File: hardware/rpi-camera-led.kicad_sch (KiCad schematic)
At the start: 20 parts, among them J1 FFC 15P 1.0mm bottom contact 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, J2 FFC 15P 1.0mm top contact (to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, J3 Qwiic (JST SH 1.0mm), J4 SWD program header 2.54mm, Q1 AO3400A, Q2 Phototransistor, U1 CH32V003A4M6

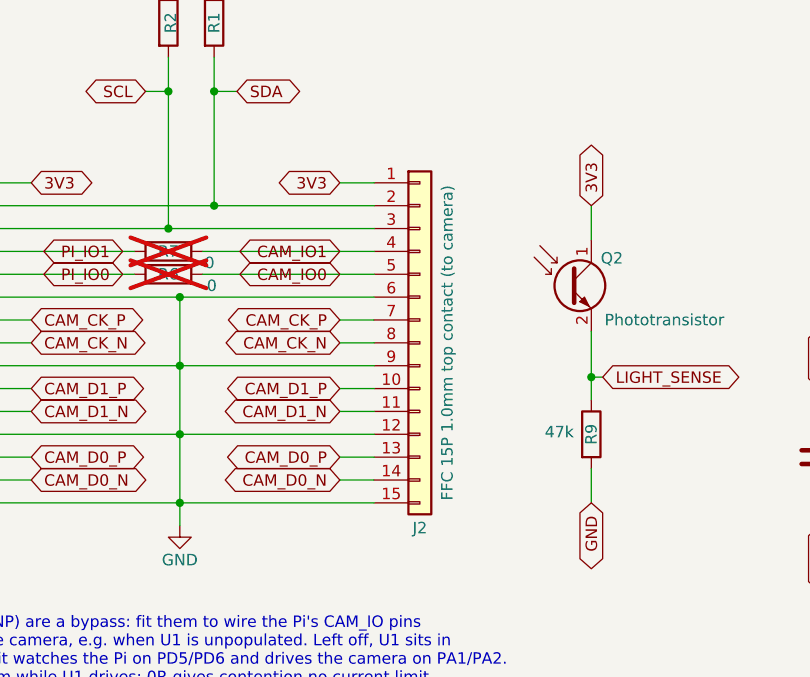
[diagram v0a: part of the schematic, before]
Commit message: Tim's KiCad session: six straight MIPI runs, J2 re-mirrored
Committing the working files as they stand so the routing is not lost.
This is an inconsistent intermediate state, recorded rather than
tidied, because the two halves disagree:

  * Six straight traces on F.Cu, 0.2mm, each a full 12.6mm run at
    constant Y from J1's pad column to J2's -- the MIPI pairs and
    clock, exactly the payoff the alignment work was for.
  * J2 carries (mirror x) again, which puts the connector mapping back
    to J1.k <-> J2.k and undoes be3c223.

Straight runs need the reversed mapping, so with the mirror back five
of the six traces land on a pad of the wrong net: CAM_CK_P on J2.7
(GND), CAM_D0_N on J2.14 (SDA), CAM_D0_P on J2.13 (SCL), CAM_D1_N on
J2.11 (CAM_IO0), CAM_D1_P on J2.10 (GND).  Only CAM_CK_N is right, pin
8 being the one pin where both mappings agree.  Hence DRC 93 -> 111 and
one net fewer unconnected.

Everything else from the recent commits survived the save, so this
looks like the schematic editor writing back a buffer loaded before
be3c223 rather than a decision.

Co-Authored-By: Claude Opus 5 (1M context) <noreply@anthropic.com>
Claude-Session: https://claude.ai/code/session_01E6VQHygrbAGSqdngQQsBdx
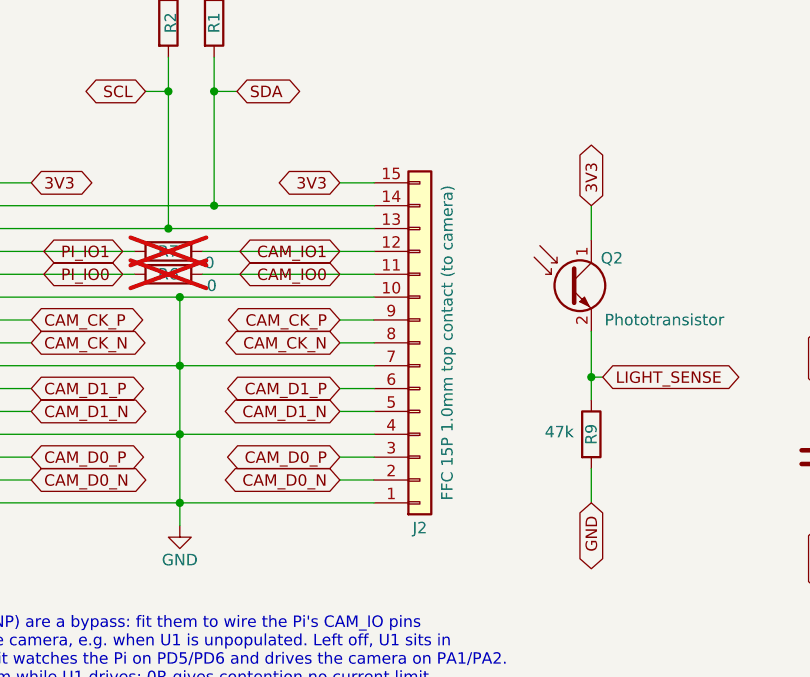
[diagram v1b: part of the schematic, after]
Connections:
- net 3V3: now also J2.15 (Pin_15); no longer J2.1 (Pin_1)
- net CAM_CK_P: now also J2.9 (Pin_9); no longer J2.7 (Pin_7)
- net CAM_D0_N: now also J2.2 (Pin_2); no longer J2.14 (Pin_14)
- net CAM_D0_P: now also J2.3 (Pin_3); no longer J2.13 (Pin_13)
- net CAM_D1_N: now also J2.5 (Pin_5); no longer J2.11 (Pin_11)
- net CAM_D1_P: now also J2.6 (Pin_6); no longer J2.10 (Pin_10)
- net CAM_IO0: now also J2.11 (Pin_11); no longer J2.5 (Pin_5)
- net CAM_IO1: now also J2.12 (Pin_12); no longer J2.4 (Pin_4)
- net GND: now also J2.1 (Pin_1), J2.10 (Pin_10), J2.4 (Pin_4), J2.7 (Pin_7); no longer J2.12 (Pin_12), J2.15 (Pin_15), J2.6 (Pin_6), J2.9 (Pin_9)
- net SCL: now also J2.13 (Pin_13); no longer J2.3 (Pin_3)
- net SDA: now also J2.14 (Pin_14); no longer J2.2 (Pin_2)
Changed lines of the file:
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@@
 		)
 	)
+	(text "J1 and J2 are deliberately different parts: J1 bottom contact, J2 top contact.\nTop contact mirrors J2's cable-to-pad order, which cancels the 180 deg rotation\nbetween two connectors whose cables leave opposite edges -- so every J1->J2 net\nruns straight across on one layer instead of crossing the whole bus.\nCost: the camera-side cable goes in contacts up, i.e. flipped from the Pi side.\nUse an opposite-side (type D) FFC there, or fold a standard same-side one."
+		(exclude_from_sim no)
+		(at 181.61 149.86 0)
+		(effects
+			(font
+				(size 1.27 1.27)
+			)
+			(justify left bottom)
+		)
+	)
 	(text "SOP-16 bonds no two ports to one pin, so PD1/SWIO is programming only\nand PC3/T1CH3 drives the LED gate: no LED flicker while flashing firmware.\nPC6, PC7, PD4 and PC0 are spare. PD7 is left unused on purpose: it is NRST\nuntil the RST_MODE option byte says otherwise, so a Pi GPIO on it would\nreset the MCU on a factory-fresh part."
 		(exclude_from_sim no)
@@
 		(at 160.02 52.07)
 	)
+	(no_connect
+		(at 160.02 59.69)
+	)
 	(wire
 		(pts
@@
 	(wire
 		(pts
+			(xy 160.02 54.61) (xy 163.83 54.61)
+		)
+		(stroke
+			(width 0)
+			(type default)
+		)
+	)
+	(wire
+		(pts
 			(xy 27.94 74.93) (xy 43.18 74.93)
 		)
@@
 		)
 	)
+	(global_label "PI_IO1"
+		(shape bidirectional)
+		(at 163.83 54.61 0)
+		(fields_autoplaced yes)
+		(effects
+			(font
+				(size 1.27 1.27)
+			)
+			(justify left)
+		)
+		(property "Intersheetrefs" "${INTERSHEET_REFS}"
+			(at 173.9137 54.61 0)
+			(effects
+				(font
+					(size 1.27 1.27)
+				)
+				(justify left)
+				(hide yes)
+			)
+		)
+	)
 	(global_label "GND"
 		(shape bidirectional)
@@
 		(lib_id "Connector_Generic:Conn_01x15")
 		(at 74.93 82.55 0)
+		(mirror x)
 		(unit 1)
 		(exclude_from_sim no)
@@
 	)
 	(embedded_fonts no)
-	(wire
-		(pts
-			(xy 160.02 54.61) (xy 163.83 54.61)
-		)
-		(stroke
-			(width 0)
-			(type default)
-		)
-	)
-	(global_label "PI_IO1"
-		(shape bidirectional)
-		(at 163.83 54.61 0)
-		(fields_autoplaced yes)
-		(effects
-			(font
-				(size 1.27 1.27)
-			)
-			(justify left)
-		)
-		(property "Intersheetrefs" "${INTERSHEET_REFS}"
-			(at 173.9137 54.61 0)
-			(effects
-				(font
-					(size 1.27 1.27)
-				)
-				(justify left)
-				(hide yes)
-			)
-		)
-	)
-	(no_connect
-		(at 160.02 59.69)
-	)
-	(text "J1 and J2 are deliberately different parts: J1 bottom contact, J2 top contact.\nTop contact mirrors J2's cable-to-pad order, which cancels the 180 deg rotation\nbetween two connectors whose cables leave opposite edges -- so every J1->J2 net\nruns straight across on one layer instead of crossing the whole bus.\nCost: the camera-side cable goes in contacts up, i.e. flipped from the Pi side.\nUse an opposite-side (type D) FFC there, or fold a standard same-side one."
-		(exclude_from_sim no)
-		(at 181.61 149.86 0)
-		(effects
-			(font
-				(size 1.27 1.27)
-			)
-			(justify left bottom)
-		)
-	)
 )

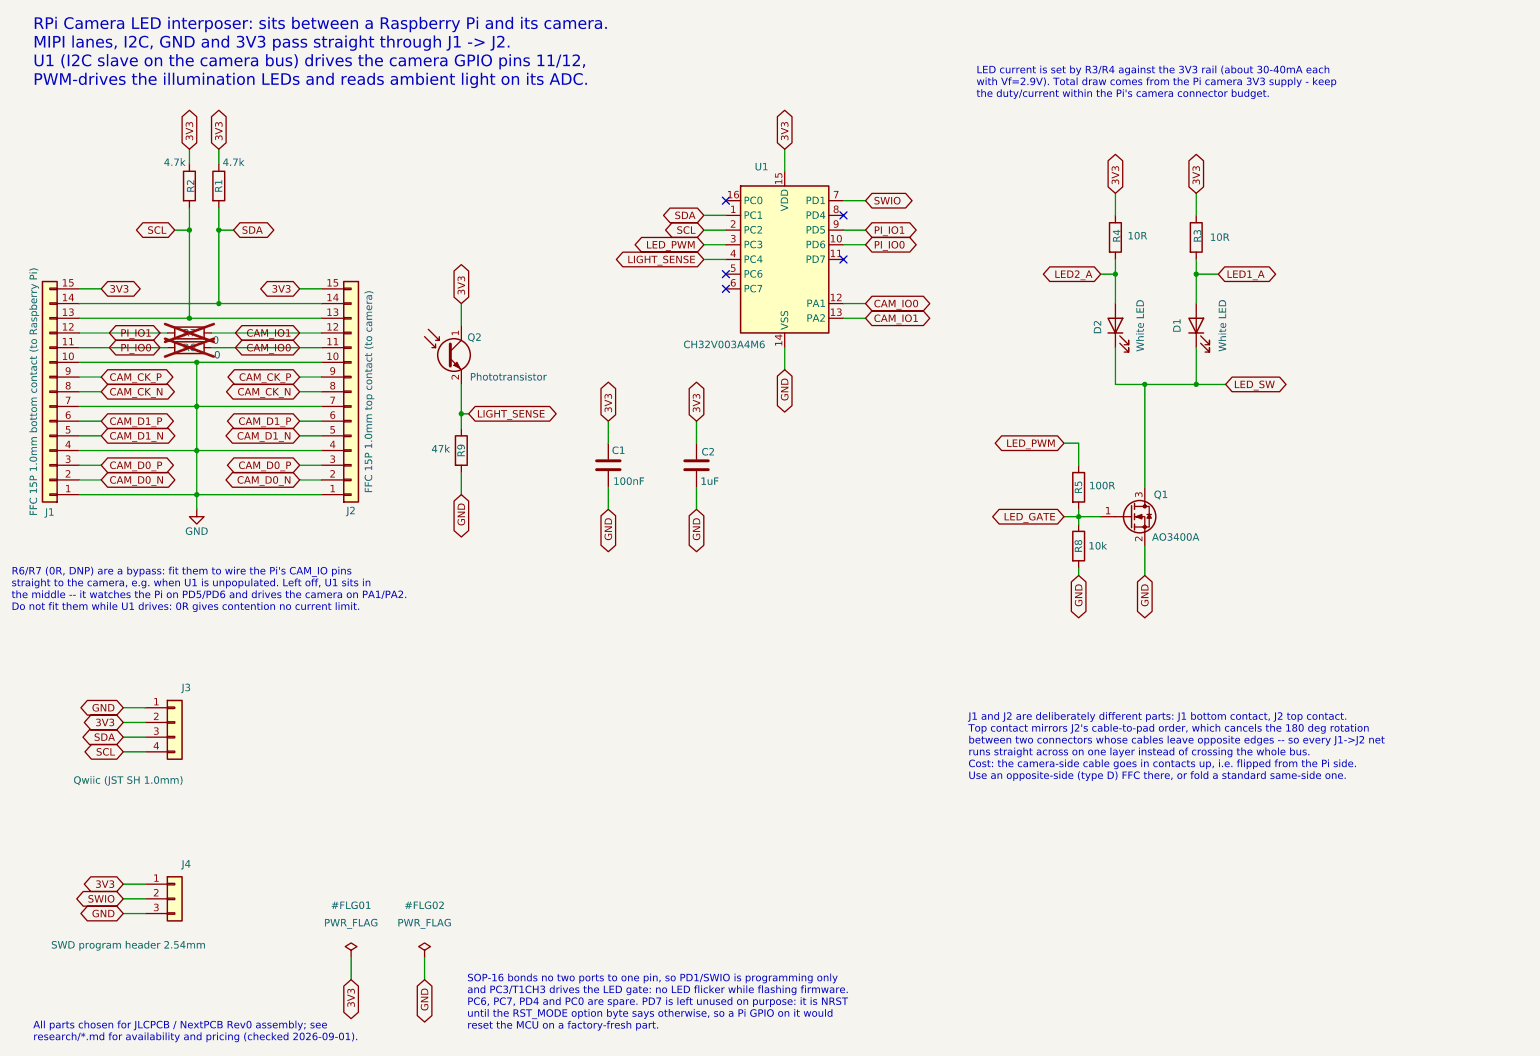
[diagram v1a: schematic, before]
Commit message: Put J2 back on the original bottom-contact part
Undo a708eef and be3c223: J1 and J2 are the same AFA07-S15FCA-00
again, wired pin-for-pin, so a standard same-side Raspberry Pi camera
cable works at both ends.  That was the real cost of the top-contact
route -- it needed an opposite-side (type D) FFC or a fold on the
camera segment, which is a poor trade for a board whose point is to sit
transparently in an existing cable run.

Everything that existed only to support the swap goes with it: the
project footprint library holding the renamed ECA copy, its
fp-lib-table, the contact-type annotations in both connectors' Value
and MPN fields, and the on-sheet note explaining why the parts
differed.  The board's embedded copy of the footprint goes back to the
stock KiCad one, pads asserted unchanged.

check_schematic.py drops the pass-through invariant, which is not
satisfiable now and would only nag: pin k is wired to pin k but faces
pin 16-k, so the bus cannot be fifteen straight traces.  Its expected
nets follow J2's pins back to the straight mapping.  check_pcb.py keeps
the facing-alignment measurement, which is still worth having -- it is
what catches a connector drifting out of mirror.

Still broken and left alone deliberately: five of the six traces in
fdd04d9 land on a pad of the wrong net, because straight runs only work
under the reversed mapping.  DRC stays at 111 violations, 49
unconnected.  They want deleting before the bus is re-routed, which is
a call for Tim rather than something to tidy away.

Co-Authored-By: Claude Opus 5 (1M context) <noreply@anthropic.com>
Claude-Session: https://claude.ai/code/session_01E6VQHygrbAGSqdngQQsBdx
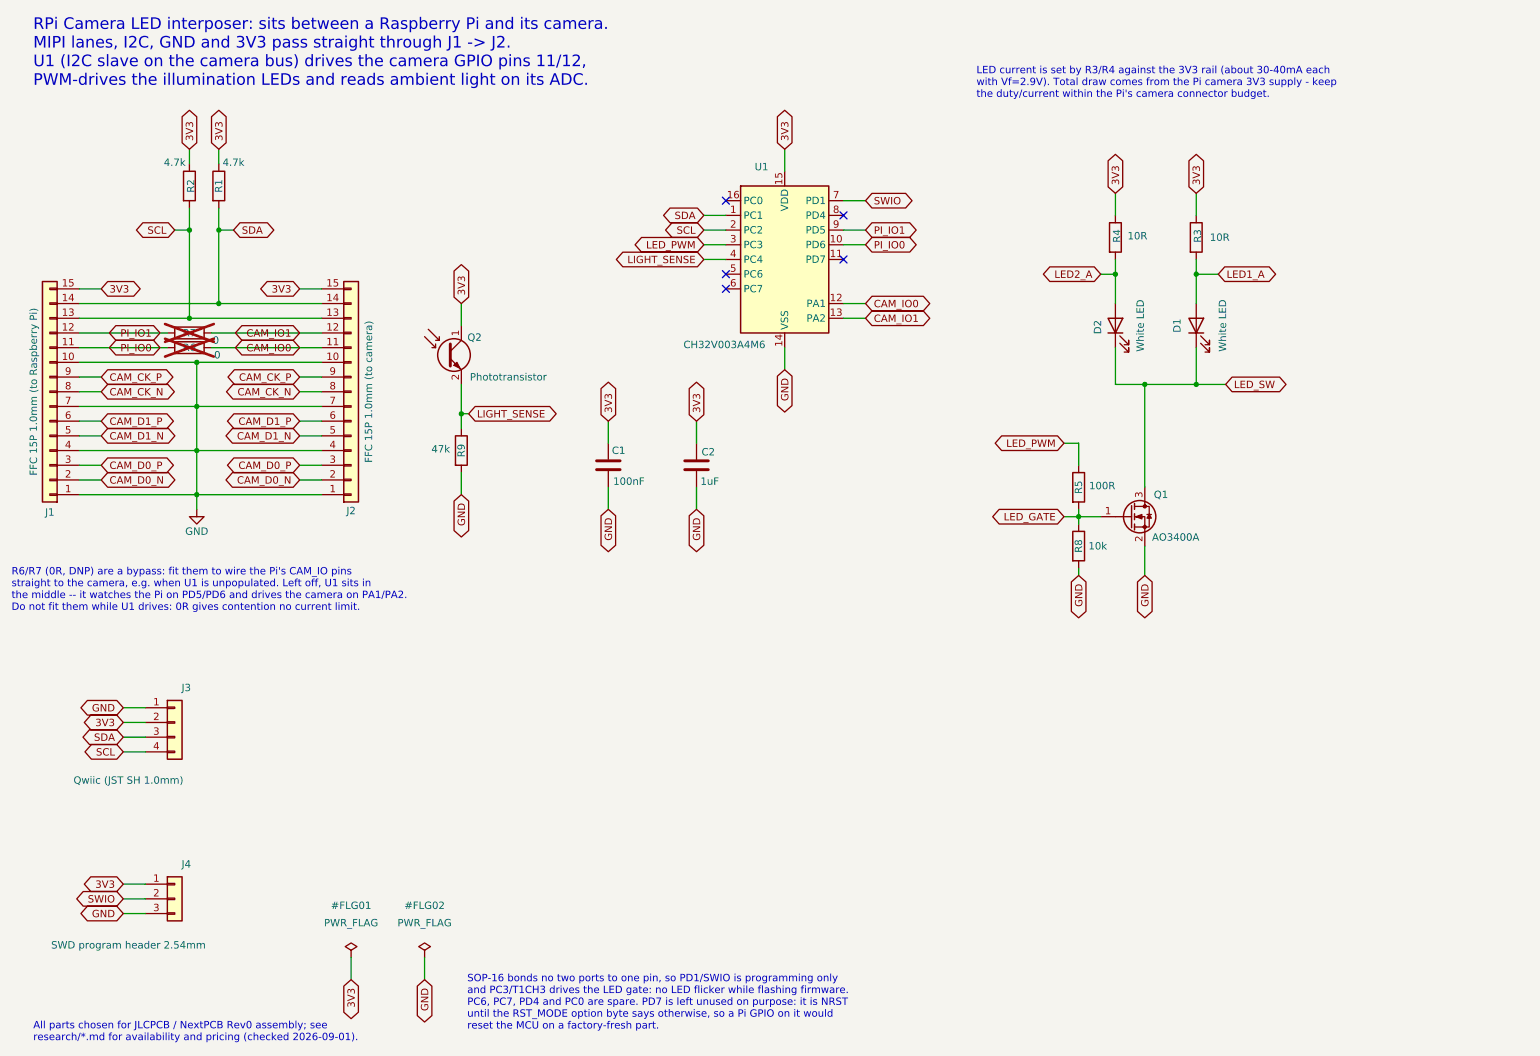
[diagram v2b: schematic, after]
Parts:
- J1: value FFC 15P 1.0mm bottom contact (to Raspberry Pi) -> FFC 15P 1.0mm (to Raspberry Pi); MPN JUSHUO AFA07-S15FCA-00 (bottom contact, LCSC C262721) -> JUSHUO AFA07-S15FCA-00 / Amphenol SFW15R-1STE1LF
- J2: value FFC 15P 1.0mm top contact (to camera) -> FFC 15P 1.0mm (to camera); footprint rpi-camera-led:JUSHUO_AFA07-S15ECA-00_1x15-1MP_P1.0mm_Horizontal -> Connector_FFC-FPC:JUSHUO_AFA07-S15FCA-00_1x15-1MP_P1.0mm_Horizontal; MPN JUSHUO AFA07-S15ECA-00 (top contact, LCSC C262742) -> JUSHUO AFA07-S15FCA-00 / Amphenol SFW15R-1STE1LF
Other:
- note removed: "J1 and J2 are deliberately different parts: J1 bottom contact, J2 top contact. Top contact mirrors J2's cable-to-pad order, which cancels the 180 deg rotation between two connectors whose cables leave opposite edges -- so every J1->J2 net runs straight across on one layer instead of crossing the whole bus. Cost: the camera-side cable goes in contacts up, i.e. flipped from the Pi side. Use an oppo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"
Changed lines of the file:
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@@
 		)
 	)
-	(text "J1 and J2 are deliberately different parts: J1 bottom contact, J2 top contact.\nTop contact mirrors J2's cable-to-pad order, which cancels the 180 deg rotation\nbetween two connectors whose cables leave opposite edges -- so every J1->J2 net\nruns straight across on one layer instead of crossing the whole bus.\nCost: the camera-side cable goes in contacts up, i.e. flipped from the Pi side.\nUse an opposite-side (type D) FFC there, or fold a standard same-side one."
-		(exclude_from_sim no)
-		(at 181.61 149.86 0)
-		(effects
-			(font
-				(size 1.27 1.27)
-			)
-			(justify left bottom)
-		)
-	)
 	(text "SOP-16 bonds no two ports to one pin, so PD1/SWIO is programming only\nand PC3/T1CH3 drives the LED gate: no LED flicker while flashing firmware.\nPC6, PC7, PD4 and PC0 are spare. PD7 is left unused on purpose: it is NRST\nuntil the RST_MODE option byte says otherwise, so a Pi GPIO on it would\nreset the MCU on a factory-fresh part."
 		(exclude_from_sim no)
@@
 			)
 		)
-		(property "Value" "FFC 15P 1.0mm top contact (to camera)"
+		(property "Value" "FFC 15P 1.0mm (to camera)"
 			(at 77.978 82.55 90)
 			(effects
@@
 			)
 		)
-		(property "Footprint" "rpi-camera-led:JUSHUO_AFA07-S15ECA-00_1x15-1MP_P1.0mm_Horizontal"
+		(property "Footprint" "Connector_FFC-FPC:JUSHUO_AFA07-S15FCA-00_1x15-1MP_P1.0mm_Horizontal"
 			(at 74.93 82.55 0)
 			(effects
@@
 			)
 		)
-		(property "MPN" "JUSHUO AFA07-S15ECA-00 (top contact, LCSC C262742)"
+		(property "MPN" "JUSHUO AFA07-S15FCA-00 / Amphenol SFW15R-1STE1LF"
 			(at 74.93 82.55 0)
 			(effects
@@
 			)
 		)
-		(property "Value" "FFC 15P 1.0mm bottom contact (to Raspberry Pi)"
+		(property "Value" "FFC 15P 1.0mm (to Raspberry Pi)"
 			(at 20.066 82.55 90)
 			(effects
@@
 			)
 		)
-		(property "MPN" "JUSHUO AFA07-S15FCA-00 (bottom contact, LCSC C262721)"
+		(property "MPN" "JUSHUO AFA07-S15FCA-00 / Amphenol SFW15R-1STE1LF"
 			(at 22.86 82.55 0)
 			(effects
